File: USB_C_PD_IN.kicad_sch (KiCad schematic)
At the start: 33 parts, among them IC1 TPS25730DREFR, IC8 AP7361E-33FGE-7, U1 TPS62933DRLR

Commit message: layout changes
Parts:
- removed C6, C7: 330pF, symbol Device:C
- C14, C15: footprint (none) -> Capacitor_SMD:C_0805_2012Metric; MPN (none) -> MLAST21GBB5226MTNC12
- C18: footprint (none) -> Capacitor_SMD:C_0805_2012Metric; MPN (none) -> GPC0805106-35

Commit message: layout changes
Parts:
- removed C20, C21: 4.7u, Capacitor_SMD:C_0603_1608Metric, symbol Device:C
- removed IC8: AP7361E-33FGE-7, Footprints:SON65P300X300X63-9N, symbol Symbols:AP7361E-33FGE-7
- added C22, C23: 220p, Capacitor_SMD:C_0402_1005Metric, symbol Device:C
- added C6: 10u, Capacitor_SMD:C_0402_1005Metric, symbol Device:C
- C13, C8: MPN (none) -> GPC0402106-6.3
- R11: value 198.2k -> 100k; MPN (none) -> GPR0402100K
- R20: value 198.2k -> 11k; MPN (none) -> GPR040211K
- R21: value 9.4k -> 0; MPN (none) -> GPR04020R
- R22: value 198.2k -> 10M; MPN (none) -> GPR040210M
- R23: value 162k -> 100k; MPN (none) -> GPR0402100K
- R25, R27: value 198.2k -> 18k; MPN (none) -> GPR040218R
- R26: value 190k -> 100k; MPN (none) -> GPR0402100K
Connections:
- net VIN_3V3 is gone; now on net +3V3: IC1.38 (VIN_3V3)
- net +3V3: now also C6.1
- net CC1: now also C23.1
- net CC2: now also C22.1
- net GND: now also C22.2, C23.2, C6.2
- no-connect marks 6 -> 3
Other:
- note added: "ADC1 => 2"
- note added: "ADC2 => 7"
- note added: "ADC3 => 3"
- note added: "ADC4 => 3"
- note removed: "LDO 3V 1A"
- moved on the sheet: C12, C13, C8, R11, R20, R21, R22, R27

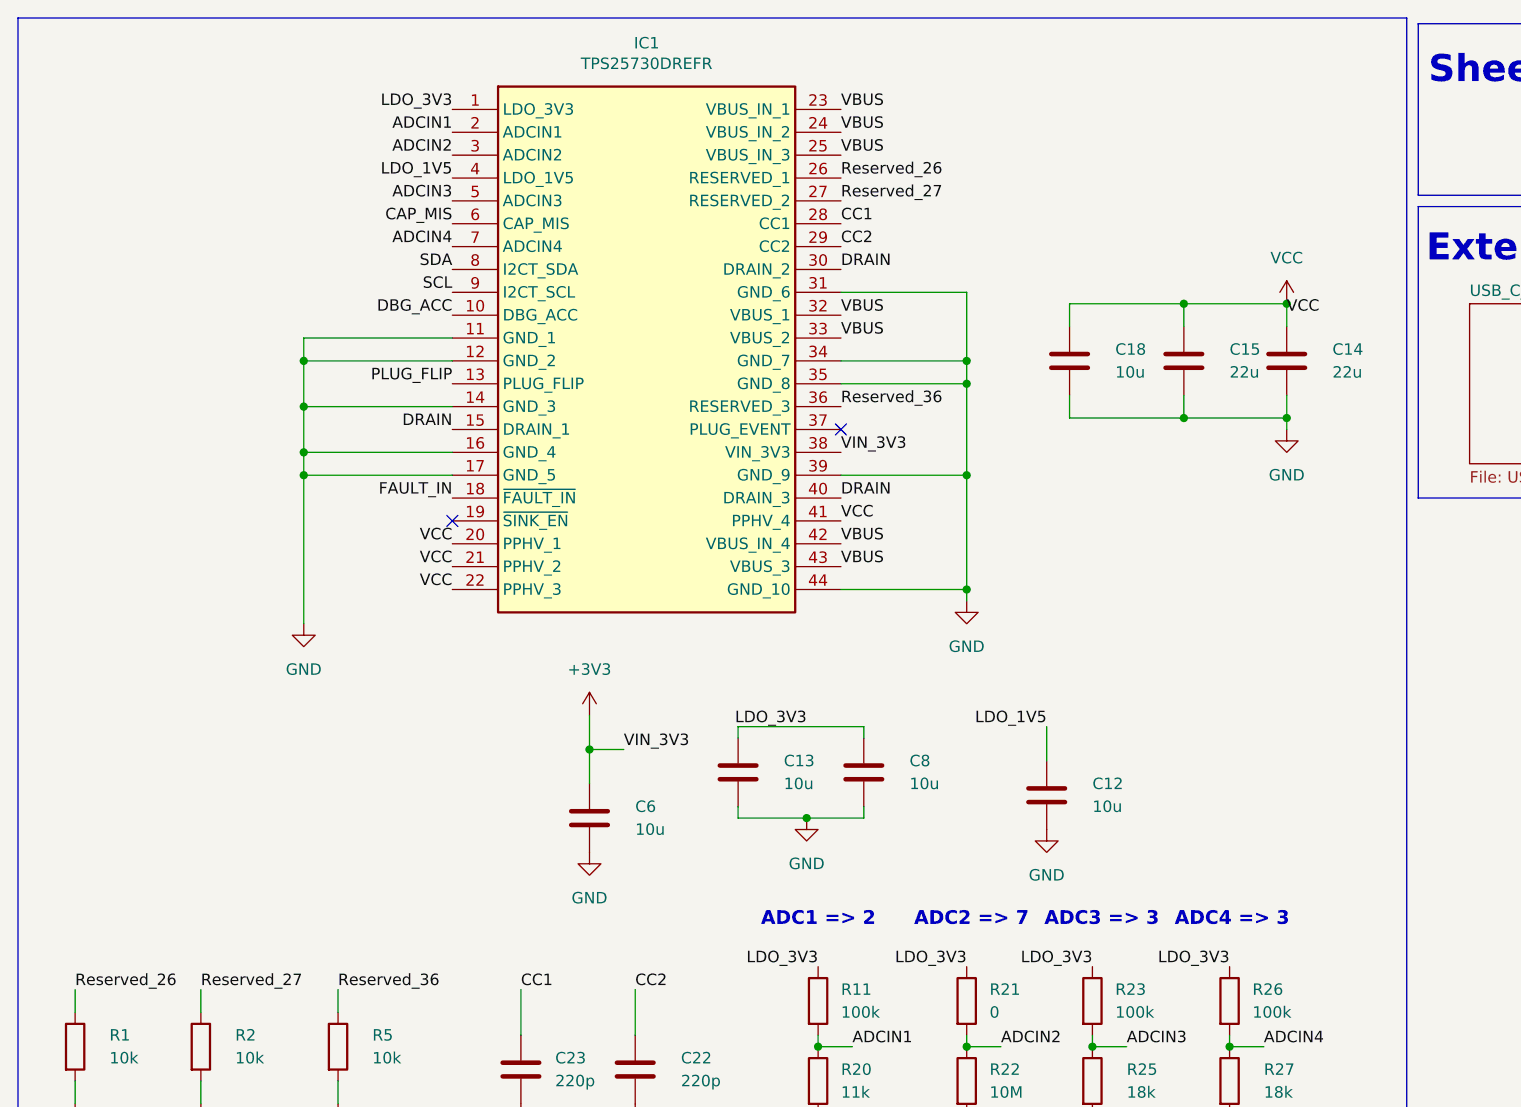
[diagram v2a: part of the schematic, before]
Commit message: Power layout changes
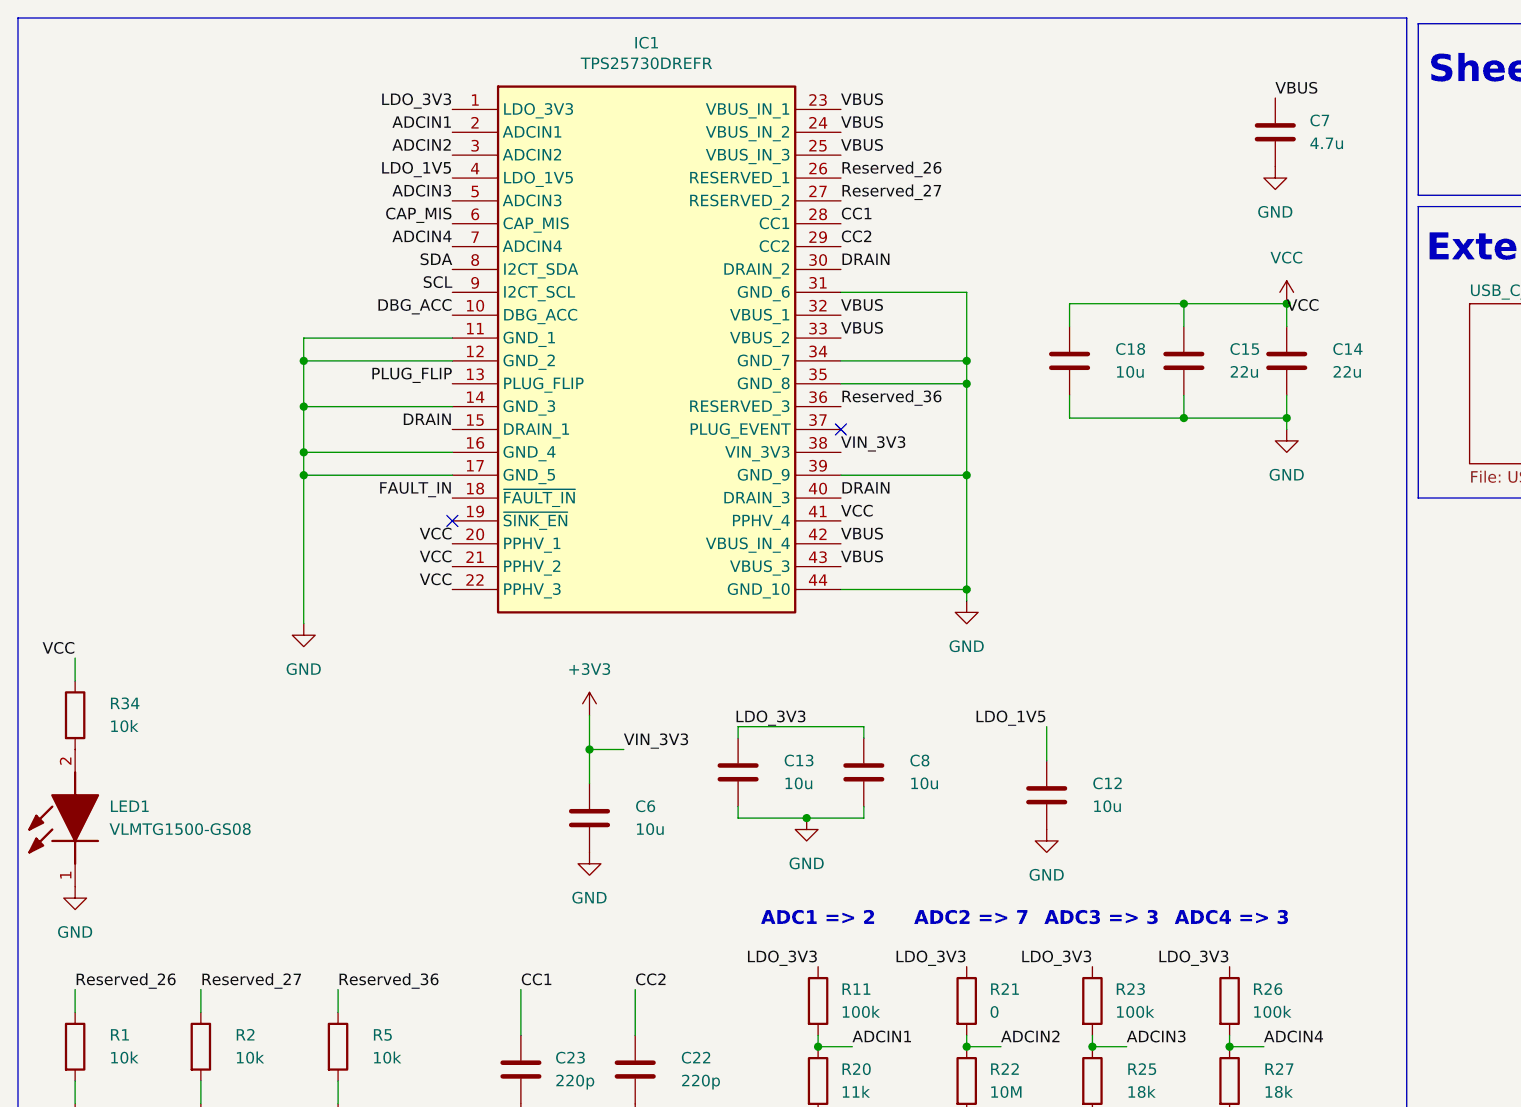
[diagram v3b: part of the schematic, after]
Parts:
- added C7: 4.7u, Capacitor_SMD:C_1206_3216Metric, symbol Device:C
- added LED1: VLMTG1500-GS08, Footprints:VLMTG1500GS08, symbol Symbols:VLMTG1500-GS08
- added R34: 10k, Resistor_SMD:R_0402_1005Metric, symbol Device:R
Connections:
- net GND: now also C7.2, LED1.1 (K)
- net VBUS: now also C7.1
- net VCC: now also R34.1
- new net: LED1.2 (A), R34.2

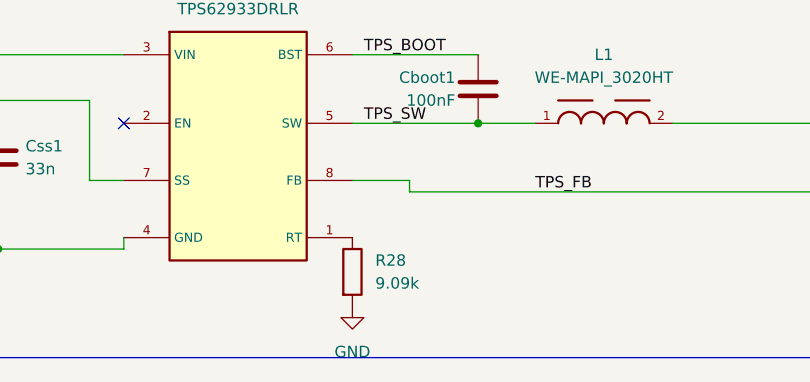
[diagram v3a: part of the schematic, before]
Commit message: Layout Changes, MPN Added
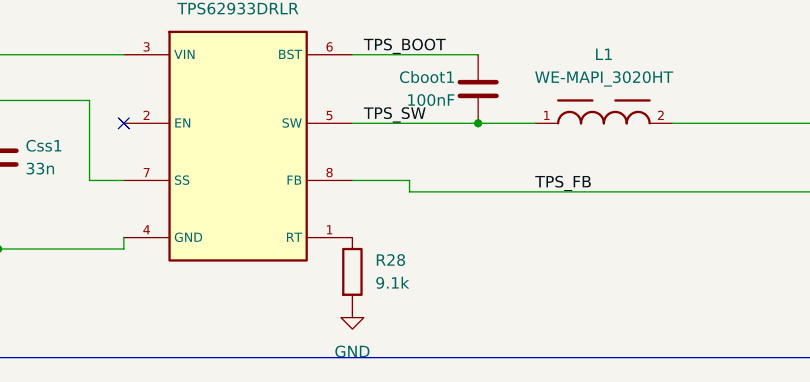
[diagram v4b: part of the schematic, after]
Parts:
- C12: MPN (none) -> GPC0402106-6.3
- C22, C23: CPN GPC0402221-10 -> (none); MPN (none) -> GPC0402221-10
- C6: CPN GPC0402106-6.3 -> (none); MPN (none) -> GPC0402106-6.3
- IC1: MPN (none) -> TPS25730DREFR
- LED1: MPN (none) -> VLMTG1500-GS08
- R1, R2, R34, R5: MPN (none) -> GPR040210K
- R28: value 9.09k -> 9.1k; MPN (none) -> GPR04029K1
- R4: GPN GPR040210K -> (none); MPN (none) -> GPR040210K
